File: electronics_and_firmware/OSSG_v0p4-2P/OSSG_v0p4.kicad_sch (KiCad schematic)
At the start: 42 parts, among them J1 Conn_01x05_Male, Q1 2SC4617R BR, Q2 2SC4617R BR, SW1 SW_SPST, U1 SPH0645LMH, U2 ESP32-PICO-D4, U3 CH9102F

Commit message: finished beta 2 of V0.4-2P schematic
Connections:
- net IO26: no longer TP2.1
- net IO32: no longer TP6.1
- net IO18: no longer names the net of TP11.1
- net IO18: no longer U2.35 (IO18)
- net IO4 renamed RGB
- new net ALRT: U2.35 (IO18)
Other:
- note added: "GPIO4"
- note added: "Visual Feedback RGB LEDs"
- moved on the sheet: D1, D2, D3, D4

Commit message: started work on PCB layout
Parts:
- removed D2, D3, D4: WS2812C-2020, OSSG_footprints:LED_WS2812C-2020, symbol OSSG_components_lib:WS2812C-2020
- added J?: Ext RGB, Connector_PinHeader_1.00mm:PinHeader_1x03_P1.00mm_Vertical, symbol Connector:Conn_01x03_Male
- TP12, TP13, TP14, TP5: footprint TestPoint:TestPoint_Pad_D1.0mm -> OSSG_footprints:Breakout_pads_small
- TP8, TP9: footprint OSSG_footprints:Breakout_pads -> OSSG_footprints:Breakout_pads_small
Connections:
- net +5V: now also J?.3 (Pin_3)
- net GND: now also J?.1 (Pin_1)
- net at D1.1 (Dout): now also J?.2 (Pin_2)
- no-connect marks 23 -> 22
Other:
- note added: "5V"
- note added: "Dout"

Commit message: V0.4-2P PCB nearly finished
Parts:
- removed C8: 0.1uF, Capacitor_SMD:C_0402_1005Metric, symbol Device:C_Small
- removed TP11: IO18_BO, OSSG_footprints:Breakout_pads_small, symbol Connector:TestPoint
- removed TP2: IO26_BO, OSSG_footprints:Breakout_pads_small, symbol Connector:TestPoint
- removed TP6: IO32_BO, OSSG_footprints:Breakout_pads_small, symbol Connector:TestPoint
- removed TP7: IO33_BO, OSSG_footprints:Breakout_pads_small, symbol Connector:TestPoint
- removed U1: SPH0645LMH, OSSG_footprints:SPH0645LM4H-B-SMD-GND, symbol OSSG_components_lib:SPH0645LMH
- added C1, C20: 1uF, Capacitor_SMD:C_0402_1005Metric, symbol Device:C_Small
- added J4: Touch, OSSG_footprints:Solder-2P-Connector, symbol Connector:Conn_01x02_Male
- added R1: 10K, Resistor_SMD:R_0402_1005Metric, symbol Device:R_Small
- added U1: MP23DB01HPTR, OSSG_footprints:MP23DB01HPTR, symbol OSSG_components_lib:MP23DB01HPTR
- C4: renamed from C2; value 1uF -> 100nF
- J1: footprint Connector_PinHeader_1.00mm:PinHeader_1x05_P1.00mm_Horizontal -> OSSG_footprints:Solder-5P-Connector
- J2: renamed from J?; footprint Connector_PinHeader_1.00mm:PinHeader_1x03_P1.00mm_Vertical -> OSSG_footprints:Solder-3P-Connector
- SW1: footprint Button_Switch_SMD:SW_SPST_B3U-3000P-B -> OSSG_footprints:SMD_Switch_Panasonic_EVQPUL_EVQPUC_6.3x6.7; LCSCLink https://lcsc.com/product-detail/Tactile-Switches_Omron-Elec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 -> (none); MPN SW1103CT-ND -> UK-B0249-SP25Y; MPN_LCSC C306884 -> C493280; Price 1.49 -> (none); Price_LCSSC 0.8963 -> (none)
- TP12: value IO0_TP -> IO0; footprint OSSG_footprints:Breakout_pads_small -> OSSG_footprints:Breakout_pads_very_small
- TP13: value TXIN -> Tx; footprint OSSG_footprints:Breakout_pads_small -> OSSG_footprints:Breakout_pads_very_small
- TP14: value RXIN -> Rx; footprint OSSG_footprints:Breakout_pads_small -> OSSG_footprints:Breakout_pads_very_small
- TP5: footprint OSSG_footprints:Breakout_pads_small -> OSSG_footprints:Breakout_pads_very_small
- TP8: value +3.3V_BO -> 3V3
- TP9: value GND_BO -> GND
- renumbered C1 to C2, C4 to C5, C5 to C6, C6 to C7, C7 to C8, R1 to R2, R2 to R3, R3 to R4, R4 to R5, R5 to R6
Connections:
- net IO14 is gone; now on net RGB: U2.17 (IO14)
- net +3V3: now also C5.1, C6.1, R1.2, U1.5 (VDD)
- net +5V: now also C20.1
- net ADC1C0: no longer U2.6 (SENSOR_CAPP)
- net ALRT: now also U2.42 (IO21); no longer U2.35 (IO18)
- net EN: now also C1.1, R1.1; no longer C4.1, R4.1, SW1.2 (B)
- net GND: now also SW1.2 (B), C1.2, C20.2, J4.1 (Pin_1), U1.3 (GND); no longer SW1.1 (A)
- net IO25: no longer U2.14 (IO25)
- net IO9: no longer J1.5 (Pin_5)
- net RGB: no longer U2.24 (IO4)
- net at R2.1, R3.2: now also U1.2 (L/R)
- net ADC1C2 renamed SWITCH
- net SWITCH: now also C4.1, R4.1, SW1.1 (A)
- net IO2 renamed TOUCH1
- net TOUCH1: now also J4.2 (Pin_2)
- net IO21 renamed i2S2_CLK
- net i2S2_CLK: now also U2.14 (IO25); no longer U2.42 (IO21)
- net IO23: no longer names the net of U2.36 (IO23)
- net IO23: no longer J1.4 (Pin_4)
- net IO26 renamed i2S1_Data
- net i2S1_Data: now also U1.1 (DOUT)
- net IO27: no longer names the net of U2.16 (IO27)
- net IO32 renamed i2S2_WS
- net i2S2_WS: now also J1.5 (Pin_5)
- net IO33 renamed i2S1_CLK
- net i2S1_CLK: now also U1.4 (CLK)
- net IO39 renamed i2S2_Data
- net i2S2_Data: now also J1.4 (Pin_4)
- new net SCL: U2.35 (IO18)
- new net SDA: U2.24 (IO4)
- no-connect marks 22 -> 25
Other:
- note added: "Compatible PDM Microphones: * MP23DB01HPCT Digikey: 497-MP23BD01HPCT-ND A$2.75/10 * MP23DB01HPTR Mouser: 511-MP23DB01HPTR A$2.62/10 * GMA3526H10-B26 LCSC: C498192 A$1.33/10"
- note added: "GPIO2"
- moved on the sheet: C2, C3, C4, R2, R3, R4, SW1, TP1, TP10, TP3, TP4

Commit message: EOD - PCB nearly finished
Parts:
- removed C7, C8: 0.1uF, Capacitor_SMD:C_0402_1005Metric, symbol Device:C_Small
- removed TP10: IO5_BO, OSSG_footprints:Breakout_pads_small, symbol Connector:TestPoint
- removed TP3: IO38_ADC1C1, OSSG_footprints:Breakout_pads_small, symbol Connector:TestPoint
- removed TP4: IO37_ADC1C0, OSSG_footprints:Breakout_pads_small, symbol Connector:TestPoint
- added TP2: 5V, OSSG_footprints:Breakout_pads_small, symbol Connector:TestPoint
- TP1: value IO25_BO -> IO35; footprint OSSG_footprints:Breakout_pads_small -> OSSG_footprints:Breakout_pads_very_small
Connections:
- net IO35 is gone; now on net SPARE: U2.11 (IO35)
- net +5V: now also TP2.1
- net ADC1C1: no longer names the net of U2.7 (SENSOR_CAPN)
- net IO12: no longer names the net of U2.18 (IO12)
- net IO13: no longer names the net of U2.20 (IO13)
- net IO15: no longer names the net of U2.21 (IO15)
- net IO19: no longer names the net of U2.38 (IO19)
- net IO22: no longer names the net of U2.39 (IO22)
- net IO25 renamed SPARE
- net IO34: no longer names the net of U2.10 (IO34)
- net IO5: no longer names the net of U2.34 (IO5)
- net IO9: no longer names the net of U2.28 (SD2)
- net V_USB renamed VBUS
- no-connect marks 25 -> 34
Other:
- note added: "ADC + Breakouts"
- note added: "GPIO14"
- note added: "GPIO25"
- note added: "GPIO26"
- note added: "GPIO32"
- note added: "GPIO33"
- note added: "GPIO35"
- note added: "GPIO39"
- note added: "IO36"
- note added: "IO37"
- note added: "IO38"
- note added: "IO39"
- note added: "Touch"
- note added: "User Switch"
- note removed: "ADC"
- note removed: "Filter Caps should be placed close to MCU"
- note removed: "Filters"
- note removed: "GPIO Assign"
- note removed: "GPIO4"
- moved on the sheet: J4, TP1, TP8, TP9

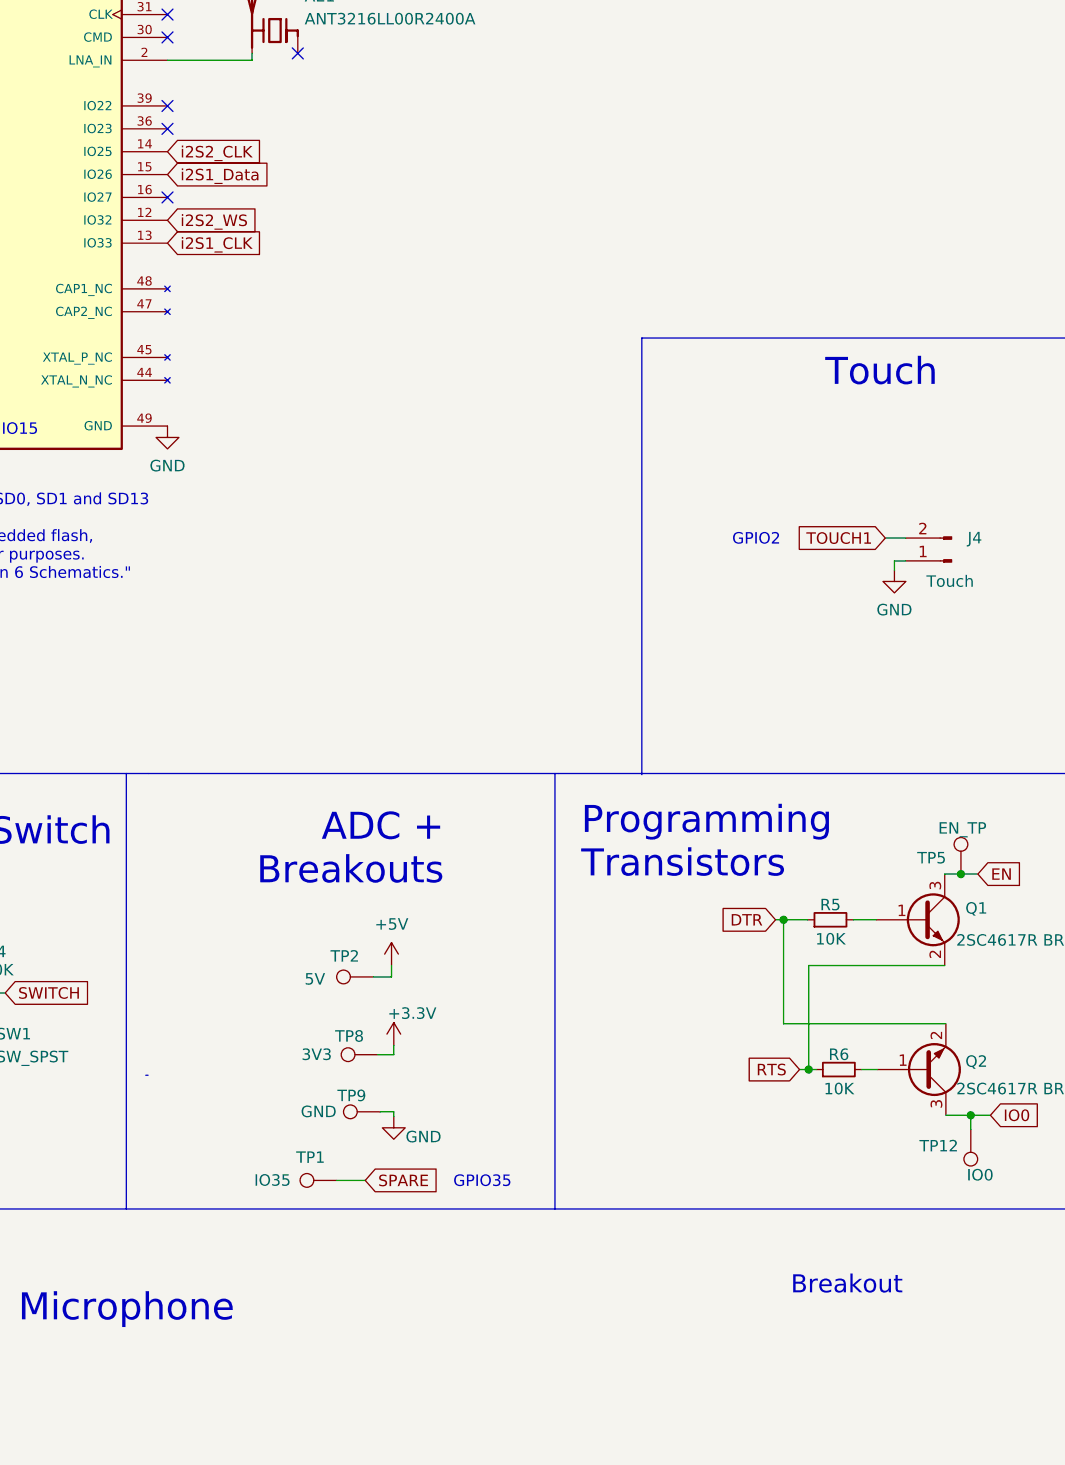
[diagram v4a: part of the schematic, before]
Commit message: V0.4 PCB nearly finished.  3D models mostly added in. Needs reviewing
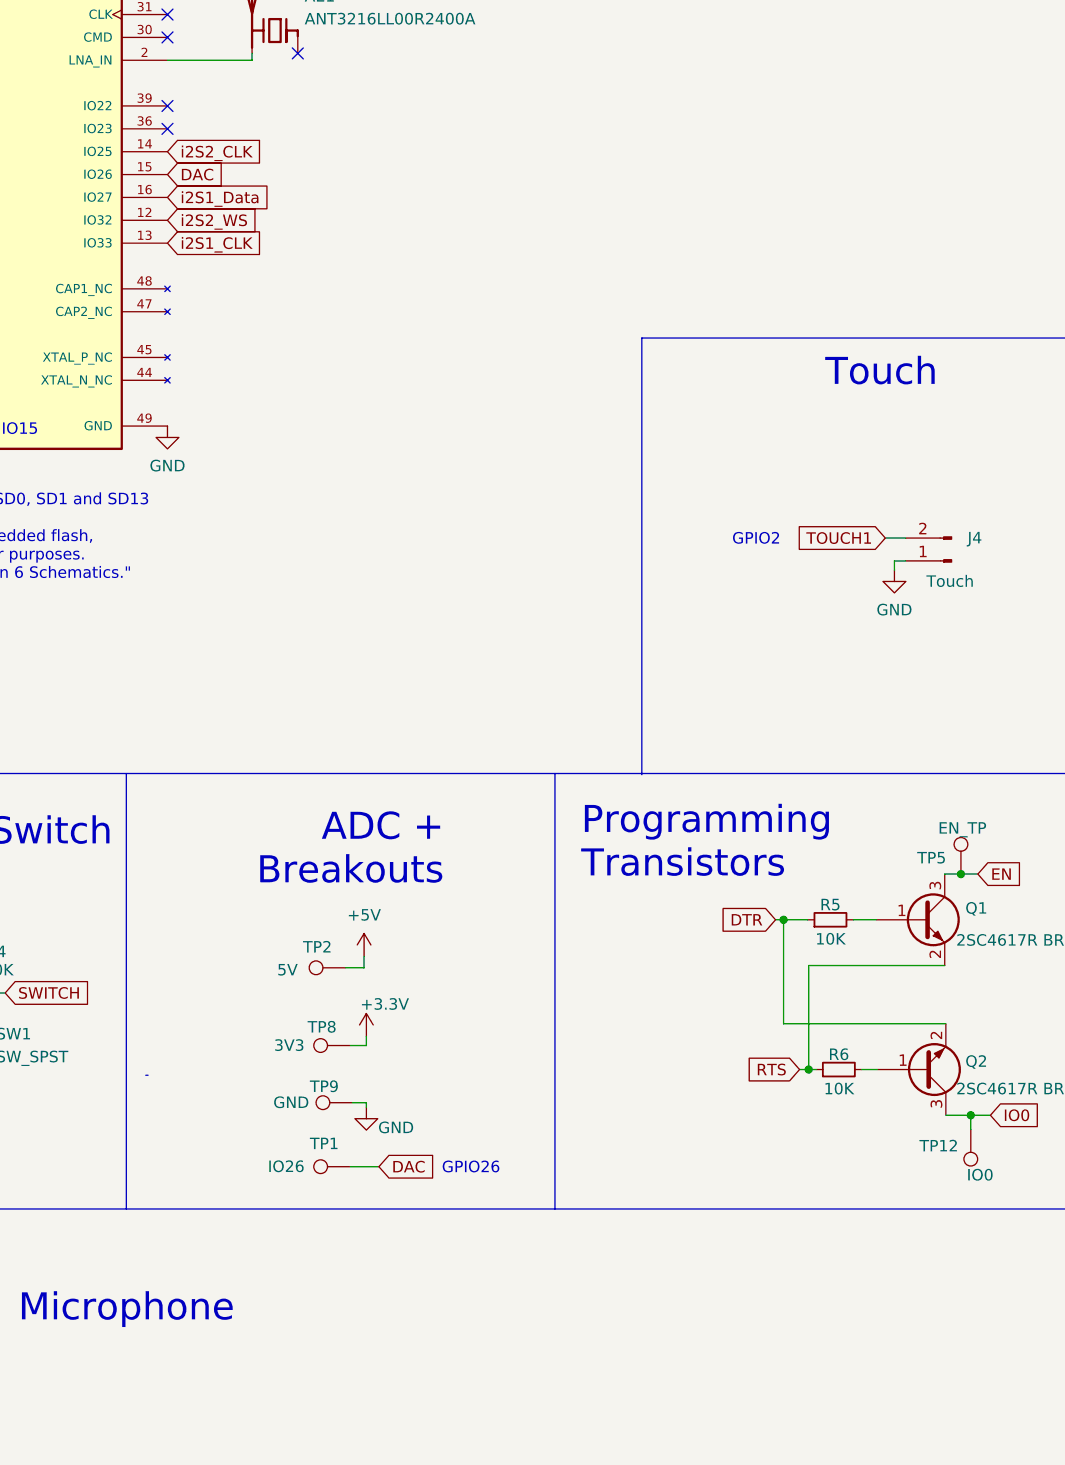
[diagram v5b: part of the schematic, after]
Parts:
- TP1: value IO35 -> IO26
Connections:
- net SPARE: no longer TP1.1
- net i2S1_Data: now also U2.16 (IO27); no longer U2.15 (IO26)
- new net DAC: TP1.1, U2.15 (IO26)
- no-connect marks 34 -> 33
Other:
- note removed: "Breakout"
- note removed: "GPIO35"
- moved on the sheet: TP1, TP2, TP8, TP9

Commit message: finished board?
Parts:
- TP5: value EN_TP -> EN
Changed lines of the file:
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@@
   (title_block
     (title "Team OpenSource Smartglasses")
-    (date "2022-09-17")
-    (rev "V0.4b3")
+    (date "2022-09-18")
+    (rev "V0.4b4")
     (company "Team Open Smart Glasses")
     (comment 1 "2P Battery Version")
@@
       (effects (font (size 1.27 1.27)) (justify left))
     )
-    (property "Value" "EN_TP" (id 1) (at 159.2834 170.434 0)
+    (property "Value" "EN" (id 1) (at 159.2834 170.434 0)
       (effects (font (size 1.27 1.27)) (justify left))
     )
@@
     )
     (path "/0b587f0b-1b6d-43da-879f-b80ff7602ce8"
-      (reference "TP5") (unit 1) (value "EN_TP") (footprint "OSSG_footprints:Breakout_pads_very_small")
+      (reference "TP5") (unit 1) (value "EN") (footprint "OSSG_footprints:Breakout_pads_very_small")
     )
     (path "/93319c92-267f-4e46-8d00-9e8e29c2c407"

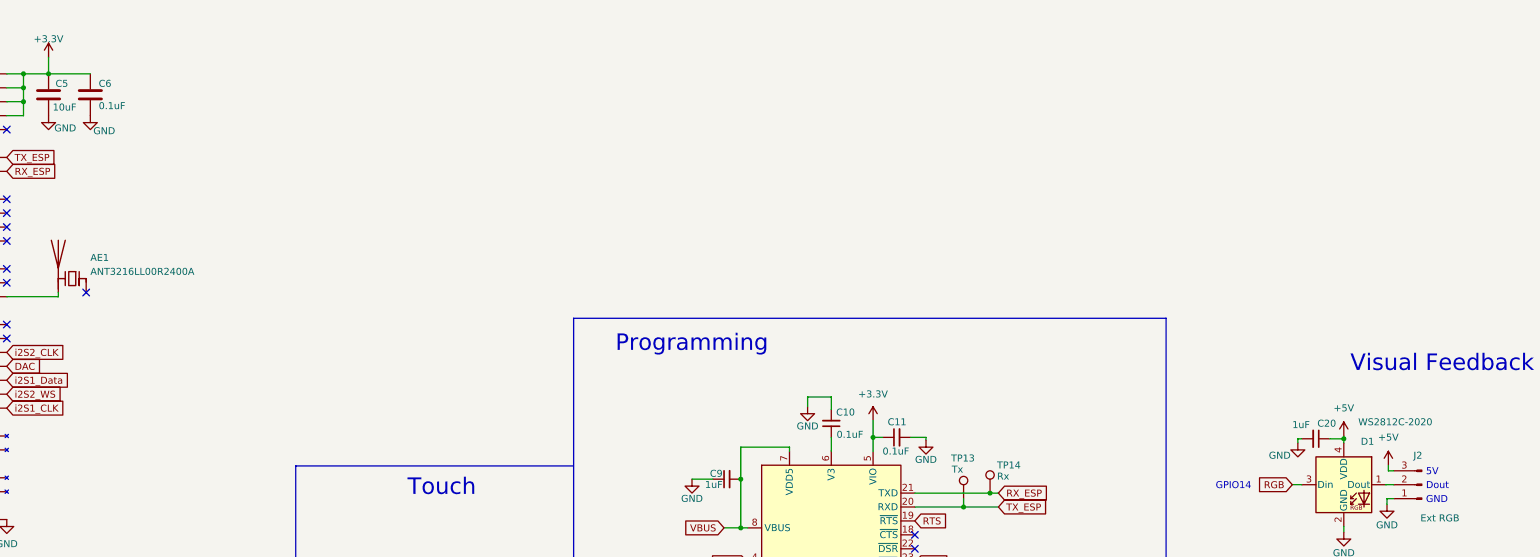
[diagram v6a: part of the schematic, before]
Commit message: adding in V0.4 BoM listings and small schematic changes
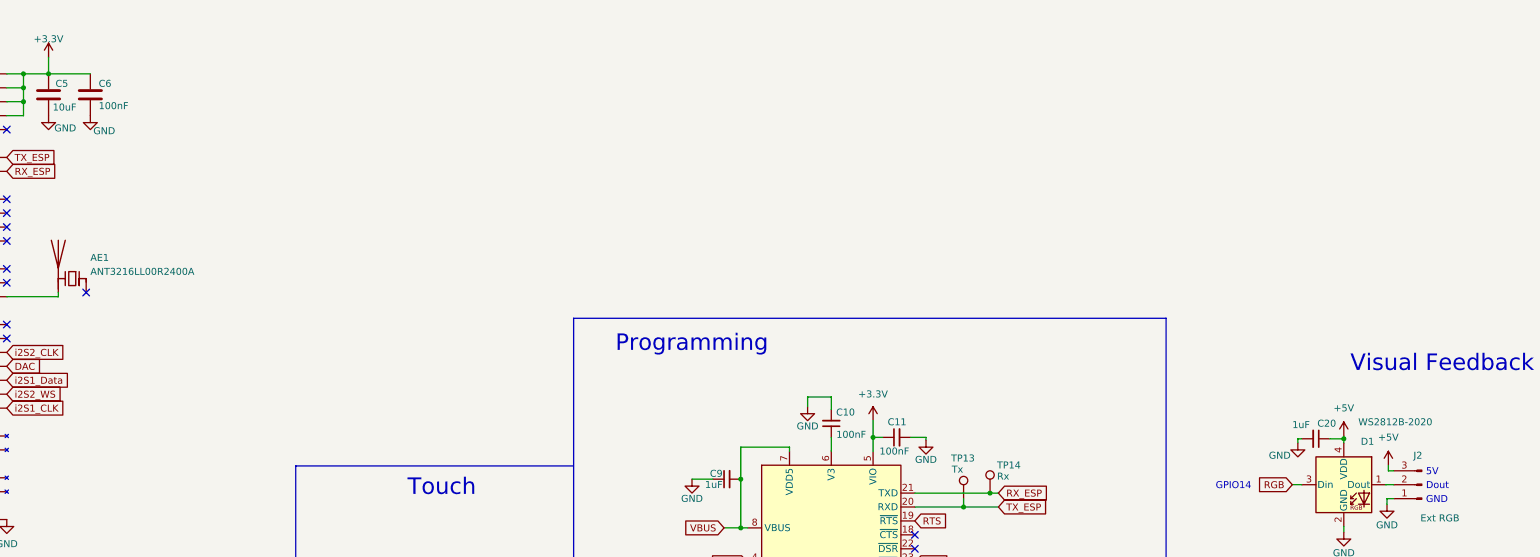
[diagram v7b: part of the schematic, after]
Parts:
- C10, C11, C6: value 0.1uF -> 100nF
- D1: value WS2812C-2020 -> WS2812B-2020
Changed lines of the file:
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@@
     (in_bom yes) (on_board yes)
     (property "Reference" "D1" (id 0) (at 321.818 111.506 0))
-    (property "Value" "WS2812C-2020" (id 1) (at 326.898 107.95 0))
+    (property "Value" "WS2812B-2020" (id 1) (at 326.898 107.95 0))
     (property "Footprint" "OSSG_footprints:LED_WS2812C-2020" (id 2) (at 318.77 127 0)
       (effects (font (size 1.27 1.27)) (justify left top) hide)
@@
       (effects (font (size 1.27 1.27)) (justify left))
     )
-    (property "Value" "0.1uF" (id 1) (at 90.424 50.292 0)
+    (property "Value" "100nF" (id 1) (at 90.424 50.292 0)
       (effects (font (size 1.27 1.27)) (justify left))
     )
@@
       (effects (font (size 1.27 1.27)) (justify left))
     )
-    (property "Value" "0.1uF" (id 1) (at 229.87 110.236 0)
+    (property "Value" "100nF" (id 1) (at 230.378 110.236 0)
       (effects (font (size 1.27 1.27)) (justify left))
     )
@@
       (effects (font (size 1.27 1.27)) (justify left))
     )
-    (property "Value" "0.1uF" (id 1) (at 238.252 113.284 90)
+    (property "Value" "100nF" (id 1) (at 238.252 113.284 90)
       (effects (font (size 1.27 1.27)) (justify left))
     )
@@
     )
     (path "/76f6f174-197c-44aa-8005-9bd143a5f8d4"
-      (reference "C6") (unit 1) (value "0.1uF") (footprint "Capacitor_SMD:C_0402_1005Metric")
+      (reference "C6") (unit 1) (value "100nF") (footprint "Capacitor_SMD:C_0402_1005Metric")
     )
     (path "/9b4a6af4-eb31-4a35-950b-5395f55e007b"
@@
     )
     (path "/a1dc9272-fc29-4dba-91bd-582737f06227"
-      (reference "C10") (unit 1) (value "0.1uF") (footprint "Capacitor_SMD:C_0402_1005Metric")
+      (reference "C10") (unit 1) (value "100nF") (footprint "Capacitor_SMD:C_0402_1005Metric")
     )
     (path "/f575c060-b888-4da8-82c5-0a40834ca894"
-      (reference "C11") (unit 1) (value "0.1uF") (footprint "Capacitor_SMD:C_0402_1005Metric")
+      (reference "C11") (unit 1) (value "100nF") (footprint "Capacitor_SMD:C_0402_1005Metric")
     )
     (path "/34a40e42-7107-4de0-9230-08b651254313/d530bc1b-b45d-4312-babc-543e1e96d4c7"
@@
     )
     (path "/34a40e42-7107-4de0-9230-08b651254313/ce48df13-61c5-4aa0-b9aa-ff53a37cf9c5"
-      (reference "C14") (unit 1) (value "22uF/16V") (footprint "Capacitor_SMD:C_0402_1005Metric")
+      (reference "C14") (unit 1) (value "22uF") (footprint "Capacitor_SMD:C_0402_1005Metric")
     )
     (path "/34a40e42-7107-4de0-9230-08b651254313/fd755c7b-cfe3-4bb9-8919-0fb8e9866eb9"
@@
     )
     (path "/422a9dcd-2106-4991-ae7d-06f03398d06d"
-      (reference "D1") (unit 1) (value "WS2812C-2020") (footprint "OSSG_footprints:LED_WS2812C-2020")
+      (reference "D1") (unit 1) (value "WS2812B-2020") (footprint "OSSG_footprints:LED_WS2812C-2020")
     )
     (path "/34a40e42-7107-4de0-9230-08b651254313/fde66a3f-8c21-48e5-a327-61734c3477b2"
@@
       (reference "Q3") (unit 1) (value "PMZ290UNE2YL") (footprint "OSSG_footprints:DFN100X60X40-3N")
     )
-    (path "/34a40e42-7107-4de0-9230-08b651254313/1fb7eba7-218f-46dd-963a-54e52ed91a0d"
-      (reference "Q4") (unit 1) (value "EMF20B02V") (footprint "OSSG_footprints:EMF20B02V")
-    )
-    (path "/34a40e42-7107-4de0-9230-08b651254313/753b2ad5-cfdc-4595-ac58-bd7e2edd8e9c"
-      (reference "Q4") (unit 2) (value "EMF20B02V") (footprint "OSSG_footprints:EMF20B02V")
+    (path "/34a40e42-7107-4de0-9230-08b651254313/c458c8e3-04c0-4379-a57e-7c63b1f8bbca"
+      (reference "Q?") (unit 1) (value "YJQD30P02A") (footprint "OSSG_footprints:EMF20B02V")
+    )
+    (path "/34a40e42-7107-4de0-9230-08b651254313/7410a3c7-5e1a-44d9-90e2-eb68c3c4ad2e"
+      (reference "Q?") (unit 2) (value "YJQD30P02A") (footprint "OSSG_footprints:EMF20B02V")
     )
     (path "/e210b962-2f1f-4e30-a861-1cd0f57e94e3"
@@
     )
     (path "/34a40e42-7107-4de0-9230-08b651254313/a005cab3-e36a-4da9-8596-7aec7f3e9a8e"
-      (reference "R7") (unit 1) (value "100k") (footprint "Resistor_SMD:R_0402_1005Metric")
+      (reference "R7") (unit 1) (value "100K") (footprint "Resistor_SMD:R_0402_1005Metric")
     )
     (path "/34a40e42-7107-4de0-9230-08b651254313/e1395c59-2f60-4b2d-bee6-e2e22b1f4ca7"
@@
     )
     (path "/34a40e42-7107-4de0-9230-08b651254313/5a92f893-7bc5-4776-be9f-3401d06ad607"
-      (reference "R16") (unit 1) (value "10k") (footprint "Resistor_SMD:R_0402_1005Metric")
+      (reference "R16") (unit 1) (value "10K") (footprint "Resistor_SMD:R_0402_1005Metric")
     )
     (path "/34a40e42-7107-4de0-9230-08b651254313/f8ba1c91-c52c-4eab-8044-ba1c3472c0fc"
